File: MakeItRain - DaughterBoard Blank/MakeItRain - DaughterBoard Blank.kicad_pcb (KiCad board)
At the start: 4 copper layers, 121.3 x 68.1 mm, 1 part, among them J1 Conn_02x15_Odd_Even

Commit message: updating some routes, updating the already done daughterboard and updating the blank layout for both.
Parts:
- J1: value Conn_02x15_Odd_Even -> Conn_02x14_Odd_Even; footprint Connector_PinHeader_2.54mm:PinHeader_2x15_P2.54mm_Vertical -> Connector_PinHeader_2.54mm:PinHeader_2x14_P2.54mm_Vertical
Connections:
- net AuxVoltage renamed SDA
- net D21 renamed D17
- net D35 renamed D26
- net D39 renamed SCL
- net D4 renamed D16
- net D5 renamed Z5
- J1 pad 10: D18 -> Z6
- J1 pad 13: +5V -> +3V3
- J1 pad 15: +5V -> +3V3
- J1 pad 16: D32 -> D23
- J1 pad 17: GND -> +3V3
- J1 pad 18: D33 -> D19
- J1 pad 20: D25 -> D18
- J1 pad 26: D0 -> TX
- J1 pad 28: TX -> RX
- J1 pad 6: D23 -> Z8
- J1 pad 8: D19 -> Z7

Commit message: MakeItRain * Main Board Fixed Routing. * replaced Opamp with the part that i can get as the old one is EOL * generated all the fab files i need. * updated the daughter plug witht eh i2c ttl flip * fixed I2C issues * DRC'ed the board
MakeItRain - DaughterBoard - Zone Expansion
* updated the daughter plug witht eh i2c ttl flip
* fixed some of the routings
* generated new fab files
* DRC'ed the board
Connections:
- J1 pad 2: SCL -> TX
- J1 pad 26: TX -> SCL
- J1 pad 28: RX -> SDA
- J1 pad 4: SDA -> RX

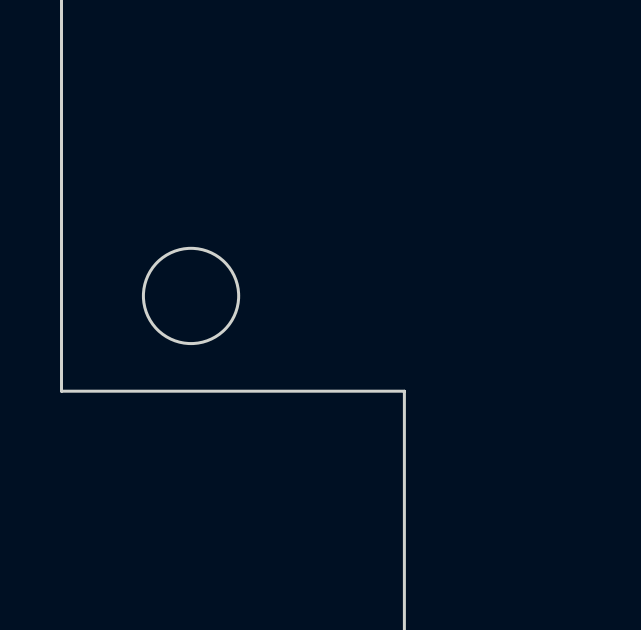
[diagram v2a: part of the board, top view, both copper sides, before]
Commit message: updating the position of one daughter board mounting holes.
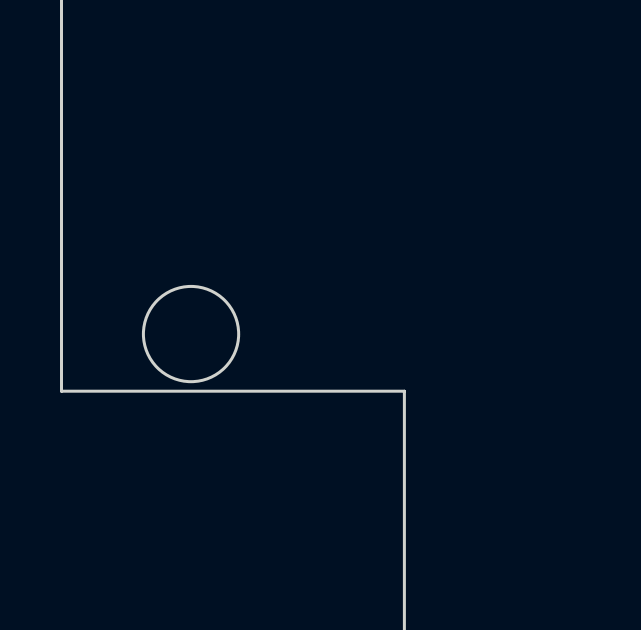
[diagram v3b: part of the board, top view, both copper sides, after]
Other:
- outline, holes or cut-outs redrawn
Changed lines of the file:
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@@
   (gr_line (start 52.07 111.76) (end 52.07 77.47)
     (stroke (width 0.1) (type solid)) (layer "Edge.Cuts"))
-  (gr_circle (center 56.388 108.585) (end 57.9755 108.585)
+  (gr_circle (center 56.388 109.855) (end 57.9755 109.855)
     (stroke (width 0.1) (type solid)) (fill none) (layer "Edge.Cuts"))
   (gr_circle (center 147.418926 108.536569) (end 149.006426 108.536569)
